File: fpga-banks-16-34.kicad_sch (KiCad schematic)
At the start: 25 parts, among them U3002 XC7K160T-FFG676, U9001 Oscillator_SMD_100MHz_ASFLMB, U9002 PCA9517A_TSSOP

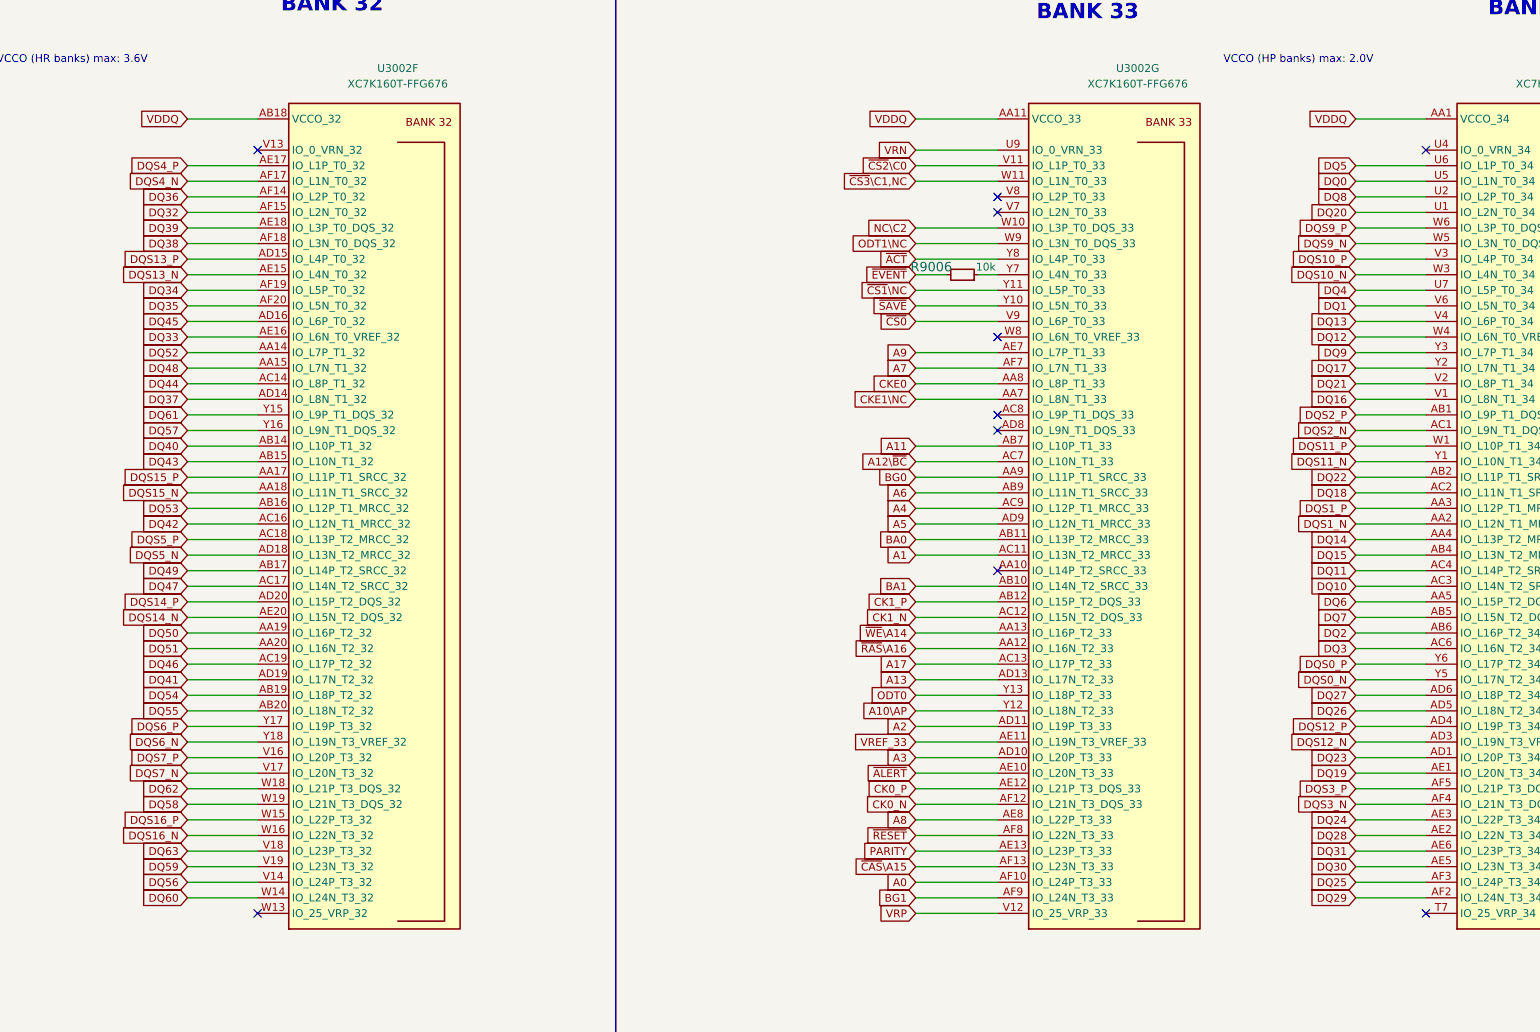
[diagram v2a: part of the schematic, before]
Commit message: Create fanout for FPGA and SODIMM, import and set PCB rules, rearange PCIE fanout to use only outer layers
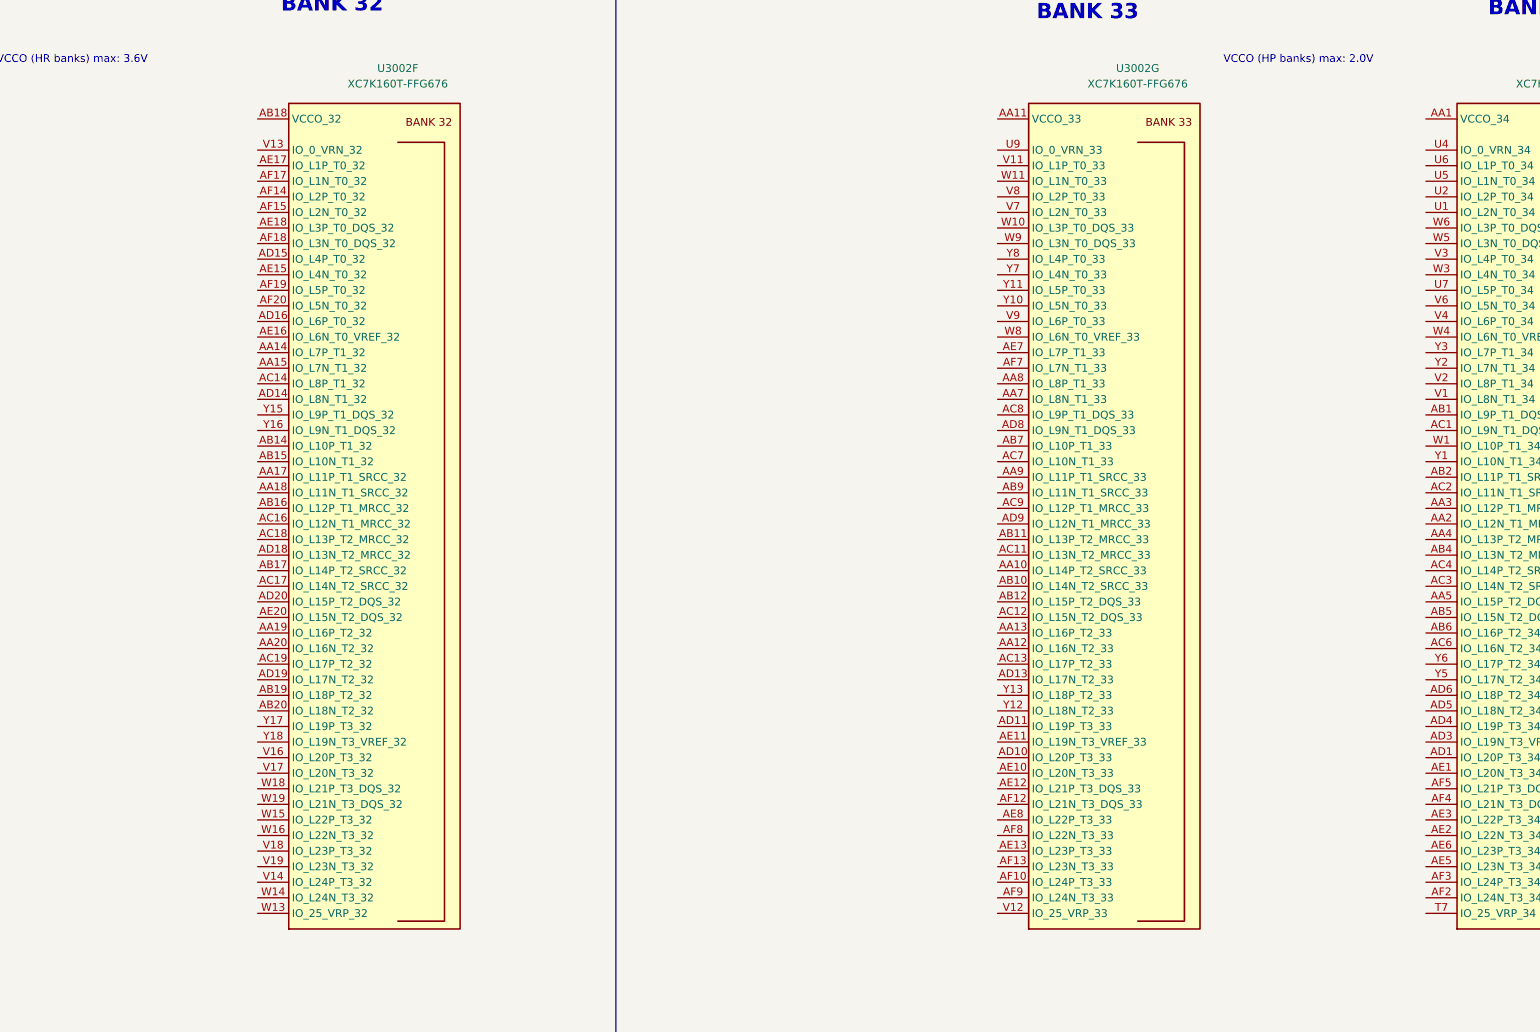
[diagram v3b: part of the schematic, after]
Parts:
- removed R9006: R_10k_0402, data-center-rdimm-ddr4-tester-footprints:R_0402_1005Metric, symbol data-center-rdimm-ddr4-tester:R_10k_0402
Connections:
- net VDDQ: no longer U3002.AA1 (VCCO_34), U3002.AA11 (VCCO_33), U3002.AB18 (VCCO_32), U3002.AB8 (VCCO_33), U3002.AC15 (VCCO_32), U3002.AC5 (VCCO_34), U3002.AD12 (VCCO_33), U3002.AD2 (VCCO_34), U3002.AE19 (VCCO_32), U3002.AE9 (VCCO_33), U3002.AF16 (VCCO_32), U3002.AF6 (VCCO_34), U3002.U3 (VCCO_34), U3002.V10 (VCCO_33), U3002.W17 (VCCO_32), U3002.W7 (VCCO_33), U3002.Y14 (VCCO_32), U3002.Y4 (VCCO_34)
- net VREF_33: no longer U3002.AE11 (IO_L19N_T3_VREF_33)
- net VRN: no longer U3002.U9 (IO_0_VRN_33)
- net VRP: no longer U3002.V12 (IO_25_VRP_33)
- net A0: no longer names the net of U3002.AF10 (IO_L24P_T3_33)
- net A1: no longer names the net of U3002.AC11 (IO_L13N_T2_MRCC_33)
- net A10\AP: no longer names the net of U3002.Y12 (IO_L18N_T2_33)
- net A11: no longer names the net of U3002.AB7 (IO_L10P_T1_33)
- net A12\~{BC}: no longer names the net of U3002.AC7 (IO_L10N_T1_33)
- net A13: no longer names the net of U3002.AD13 (IO_L17N_T2_33)
- net A17: no longer names the net of U3002.AC13 (IO_L17P_T2_33)
- net A2: no longer names the net of U3002.AD11 (IO_L19P_T3_33)
- net A3: no longer names the net of U3002.AD10 (IO_L20P_T3_33)
- net A4: no longer names the net of U3002.AC9 (IO_L12P_T1_MRCC_33)
- net A5: no longer names the net of U3002.AD9 (IO_L12N_T1_MRCC_33)
- net A6: no longer names the net of U3002.AB9 (IO_L11N_T1_SRCC_33)
- net A7: no longer names the net of U3002.AF7 (IO_L7N_T1_33)
- net A8: no longer names the net of U3002.AE8 (IO_L22P_T3_33)
- net A9: no longer names the net of U3002.AE7 (IO_L7P_T1_33)
- net BA0: no longer names the net of U3002.AB11 (IO_L13P_T2_MRCC_33)
- net BA1: no longer names the net of U3002.AB10 (IO_L14N_T2_SRCC_33)
- net BG0: no longer names the net of U3002.AA9 (IO_L11P_T1_SRCC_33)
- net BG1: no longer names the net of U3002.AF9 (IO_L24N_T3_33)
- net CK0_N: no longer names the net of U3002.AF12 (IO_L21N_T3_DQS_33)
- net CK0_P: no longer names the net of U3002.AE12 (IO_L21P_T3_DQS_33)
- net CK1_N: no longer names the net of U3002.AC12 (IO_L15N_T2_DQS_33)
- net CK1_P: no longer names the net of U3002.AB12 (IO_L15P_T2_DQS_33)
- net CKE0: no longer names the net of U3002.AA8 (IO_L8P_T1_33)
- net CKE1\NC: no longer names the net of U3002.AA7 (IO_L8N_T1_33)
- net DQ0: no longer names the net of U3002.U5 (IO_L1N_T0_34)
- net DQ1: no longer names the net of U3002.V6 (IO_L5N_T0_34)
- net DQ10: no longer names the net of U3002.AC3 (IO_L14N_T2_SRCC_34)
- net DQ11: no longer names the net of U3002.AC4 (IO_L14P_T2_SRCC_34)
- net DQ12: no longer names the net of U3002.W4 (IO_L6N_T0_VREF_34)
- net DQ13: no longer names the net of U3002.V4 (IO_L6P_T0_34)
- net DQ14: no longer names the net of U3002.AA4 (IO_L13P_T2_MRCC_34)
- net DQ15: no longer names the net of U3002.AB4 (IO_L13N_T2_MRCC_34)
- net DQ16: no longer names the net of U3002.V1 (IO_L8N_T1_34)
- net DQ17: no longer names the net of U3002.Y2 (IO_L7N_T1_34)
- net DQ18: no longer names the net of U3002.AC2 (IO_L11N_T1_SRCC_34)
- net DQ19: no longer names the net of U3002.AE1 (IO_L20N_T3_34)
- net DQ2: no longer names the net of U3002.AB6 (IO_L16P_T2_34)
- net DQ20: no longer names the net of U3002.U1 (IO_L2N_T0_34)
- net DQ21: no longer names the net of U3002.V2 (IO_L8P_T1_34)
- net DQ22: no longer names the net of U3002.AB2 (IO_L11P_T1_SRCC_34)
- net DQ23: no longer names the net of U3002.AD1 (IO_L20P_T3_34)
- net DQ24: no longer names the net of U3002.AE3 (IO_L22P_T3_34)
- net DQ25: no longer names the net of U3002.AF3 (IO_L24P_T3_34)
- net DQ26: no longer names the net of U3002.AD5 (IO_L18N_T2_34)
- net DQ27: no longer names the net of U3002.AD6 (IO_L18P_T2_34)
- net DQ28: no longer names the net of U3002.AE2 (IO_L22N_T3_34)
- net DQ29: no longer names the net of U3002.AF2 (IO_L24N_T3_34)
- net DQ3: no longer names the net of U3002.AC6 (IO_L16N_T2_34)
- net DQ30: no longer names the net of U3002.AE5 (IO_L23N_T3_34)
- net DQ31: no longer names the net of U3002.AE6 (IO_L23P_T3_34)
- net DQ32: no longer names the net of U3002.AF15 (IO_L2N_T0_32)
- net DQ33: no longer names the net of U3002.AE16 (IO_L6N_T0_VREF_32)
- net DQ34: no longer names the net of U3002.AF19 (IO_L5P_T0_32)
- net DQ35: no longer names the net of U3002.AF20 (IO_L5N_T0_32)
- net DQ36: no longer names the net of U3002.AF14 (IO_L2P_T0_32)
- net DQ37: no longer names the net of U3002.AD14 (IO_L8N_T1_32)
- net DQ38: no longer names the net of U3002.AF18 (IO_L3N_T0_DQS_32)
- net DQ39: no longer names the net of U3002.AE18 (IO_L3P_T0_DQS_32)
- net DQ4: no longer names the net of U3002.U7 (IO_L5P_T0_34)
- net DQ40: no longer names the net of U3002.AB14 (IO_L10P_T1_32)
- net DQ41: no longer names the net of U3002.AD19 (IO_L17N_T2_32)
- net DQ42: no longer names the net of U3002.AC16 (IO_L12N_T1_MRCC_32)
- net DQ43: no longer names the net of U3002.AB15 (IO_L10N_T1_32)
- net DQ44: no longer names the net of U3002.AC14 (IO_L8P_T1_32)
- net DQ45: no longer names the net of U3002.AD16 (IO_L6P_T0_32)
- net DQ46: no longer names the net of U3002.AC19 (IO_L17P_T2_32)
- net DQ47: no longer names the net of U3002.AC17 (IO_L14N_T2_SRCC_32)
- net DQ48: no longer names the net of U3002.AA15 (IO_L7N_T1_32)
- net DQ49: no longer names the net of U3002.AB17 (IO_L14P_T2_SRCC_32)
- net DQ5: no longer names the net of U3002.U6 (IO_L1P_T0_34)
- net DQ50: no longer names the net of U3002.AA19 (IO_L16P_T2_32)
- net DQ51: no longer names the net of U3002.AA20 (IO_L16N_T2_32)
- net DQ52: no longer names the net of U3002.AA14 (IO_L7P_T1_32)
- net DQ53: no longer names the net of U3002.AB16 (IO_L12P_T1_MRCC_32)
- net DQ54: no longer names the net of U3002.AB19 (IO_L18P_T2_32)
- net DQ55: no longer names the net of U3002.AB20 (IO_L18N_T2_32)
- net DQ56: no longer names the net of U3002.V14 (IO_L24P_T3_32)
- net DQ57: no longer names the net of U3002.Y16 (IO_L9N_T1_DQS_32)
- net DQ58: no longer names the net of U3002.W19 (IO_L21N_T3_DQS_32)
- net DQ59: no longer names the net of U3002.V19 (IO_L23N_T3_32)
- net DQ6: no longer names the net of U3002.AA5 (IO_L15P_T2_DQS_34)
- net DQ60: no longer names the net of U3002.W14 (IO_L24N_T3_32)
- net DQ61: no longer names the net of U3002.Y15 (IO_L9P_T1_DQS_32)
- net DQ62: no longer names the net of U3002.W18 (IO_L21P_T3_DQS_32)
- net DQ63: no longer names the net of U3002.V18 (IO_L23P_T3_32)
- net DQ7: no longer names the net of U3002.AB5 (IO_L15N_T2_DQS_34)
- net DQ8: no longer names the net of U3002.U2 (IO_L2P_T0_34)
- net DQ9: no longer names the net of U3002.Y3 (IO_L7P_T1_34)
- net DQS0_N: no longer names the net of U3002.Y5 (IO_L17N_T2_34)
- net DQS0_P: no longer names the net of U3002.Y6 (IO_L17P_T2_34)
- net DQS10_N: no longer names the net of U3002.W3 (IO_L4N_T0_34)
- net DQS10_P: no longer names the net of U3002.V3 (IO_L4P_T0_34)
- net DQS11_N: no longer names the net of U3002.Y1 (IO_L10N_T1_34)
- net DQS11_P: no longer names the net of U3002.W1 (IO_L10P_T1_34)
- net DQS12_N: no longer names the net of U3002.AD3 (IO_L19N_T3_VREF_34)
- net DQS12_P: no longer names the net of U3002.AD4 (IO_L19P_T3_34)
- net DQS13_N: no longer names the net of U3002.AE15 (IO_L4N_T0_32)
- net DQS13_P: no longer names the net of U3002.AD15 (IO_L4P_T0_32)
- net DQS14_N: no longer names the net of U3002.AE20 (IO_L15N_T2_DQS_32)
- net DQS14_P: no longer names the net of U3002.AD20 (IO_L15P_T2_DQS_32)
- net DQS15_N: no longer names the net of U3002.AA18 (IO_L11N_T1_SRCC_32)
- net DQS15_P: no longer names the net of U3002.AA17 (IO_L11P_T1_SRCC_32)
- net DQS16_N: no longer names the net of U3002.W16 (IO_L22N_T3_32)
- net DQS16_P: no longer names the net of U3002.W15 (IO_L22P_T3_32)
- net DQS1_N: no longer names the net of U3002.AA2 (IO_L12N_T1_MRCC_34)
- net DQS1_P: no longer names the net of U3002.AA3 (IO_L12P_T1_MRCC_34)
- net DQS2_N: no longer names the net of U3002.AC1 (IO_L9N_T1_DQS_34)
- net DQS2_P: no longer names the net of U3002.AB1 (IO_L9P_T1_DQS_34)
- net DQS3_N: no longer names the net of U3002.AF4 (IO_L21N_T3_DQS_34)
- net DQS3_P: no longer names the net of U3002.AF5 (IO_L21P_T3_DQS_34)
- net DQS4_N: no longer names the net of U3002.AF17 (IO_L1N_T0_32)
- net DQS4_P: no longer names the net of U3002.AE17 (IO_L1P_T0_32)
- net DQS5_N: no longer names the net of U3002.AD18 (IO_L13N_T2_MRCC_32)
- net DQS5_P: no longer names the net of U3002.AC18 (IO_L13P_T2_MRCC_32)
- net DQS6_N: no longer names the net of U3002.Y18 (IO_L19N_T3_VREF_32)
- net DQS6_P: no longer names the net of U3002.Y17 (IO_L19P_T3_32)
- net DQS7_N: no longer names the net of U3002.V17 (IO_L20N_T3_32)
- net DQS7_P: no longer names the net of U3002.V16 (IO_L20P_T3_32)
- net DQS9_N: no longer names the net of U3002.W5 (IO_L3N_T0_DQS_34)
- net DQS9_P: no longer names the net of U3002.W6 (IO_L3P_T0_DQS_34)
- net NC\C2: no longer names the net of U3002.W10 (IO_L3P_T0_DQS_33)
- net ODT0: no longer names the net of U3002.Y13 (IO_L18P_T2_33)
- net ODT1\NC: no longer names the net of U3002.W9 (IO_L3N_T0_DQS_33)
- net PARITY: no longer names the net of U3002.AE13 (IO_L23P_T3_33)
- net ~{ACT}: no longer names the net of U3002.Y8 (IO_L4P_T0_33)
- net ~{ALERT}: no longer names the net of U3002.AE10 (IO_L20N_T3_33)
- net ~{CAS}\A15: no longer names the net of U3002.AF13 (IO_L23N_T3_33)
- net ~{CS0}: no longer names the net of U3002.V9 (IO_L6P_T0_33)
- net ~{CS1}\NC: no longer names the net of U3002.Y11 (IO_L5P_T0_33)
- net ~{CS2}\C0: no longer names the net of U3002.V11 (IO_L1P_T0_33)
- net ~{CS3}\C1,NC: no longer names the net of U3002.W11 (IO_L1N_T0_33)
- net ~{RAS}\A16: no longer names the net of U3002.AA12 (IO_L16N_T2_33)
- net ~{RESET}: no longer names the net of U3002.AF8 (IO_L22N_T3_33)
- net ~{SAVE}: no longer names the net of U3002.Y10 (IO_L5N_T0_33)
- net ~{WE}\A14: no longer names the net of U3002.AA13 (IO_L16P_T2_33)
- new net: U3002.AB18 (VCCO_32), U3002.AC15 (VCCO_32), U3002.AE19 (VCCO_32), U3002.AF16 (VCCO_32), U3002.W17 (VCCO_32), U3002.Y14 (VCCO_32)
- new net: U3002.AA11 (VCCO_33), U3002.AB8 (VCCO_33), U3002.AD12 (VCCO_33), U3002.AE9 (VCCO_33), U3002.V10 (VCCO_33), U3002.W7 (VCCO_33)
- new net: U3002.AA1 (VCCO_34), U3002.AC5 (VCCO_34), U3002.AD2 (VCCO_34), U3002.AF6 (VCCO_34), U3002.U3 (VCCO_34), U3002.Y4 (VCCO_34)
- no-connect marks 43 -> 33
